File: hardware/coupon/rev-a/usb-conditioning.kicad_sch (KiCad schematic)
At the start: 18 parts, among them U24 SN74LVC2G17DBVR, U25 SN74LVC2G17DBVR, U34 TPS3808G01DBVR

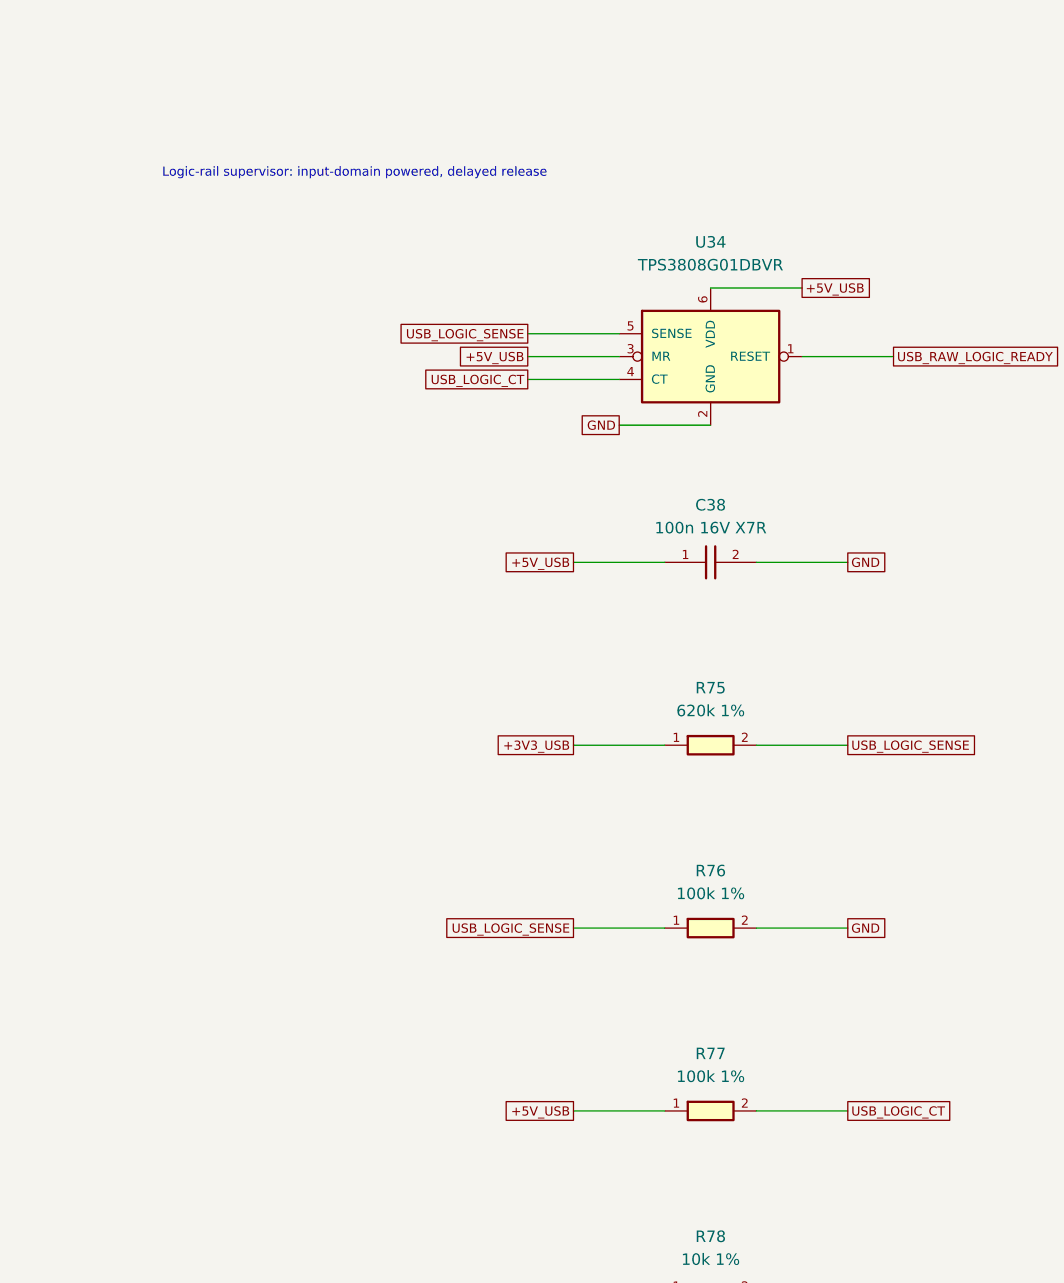
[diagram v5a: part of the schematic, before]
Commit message: Move USB supervisor to logic rail
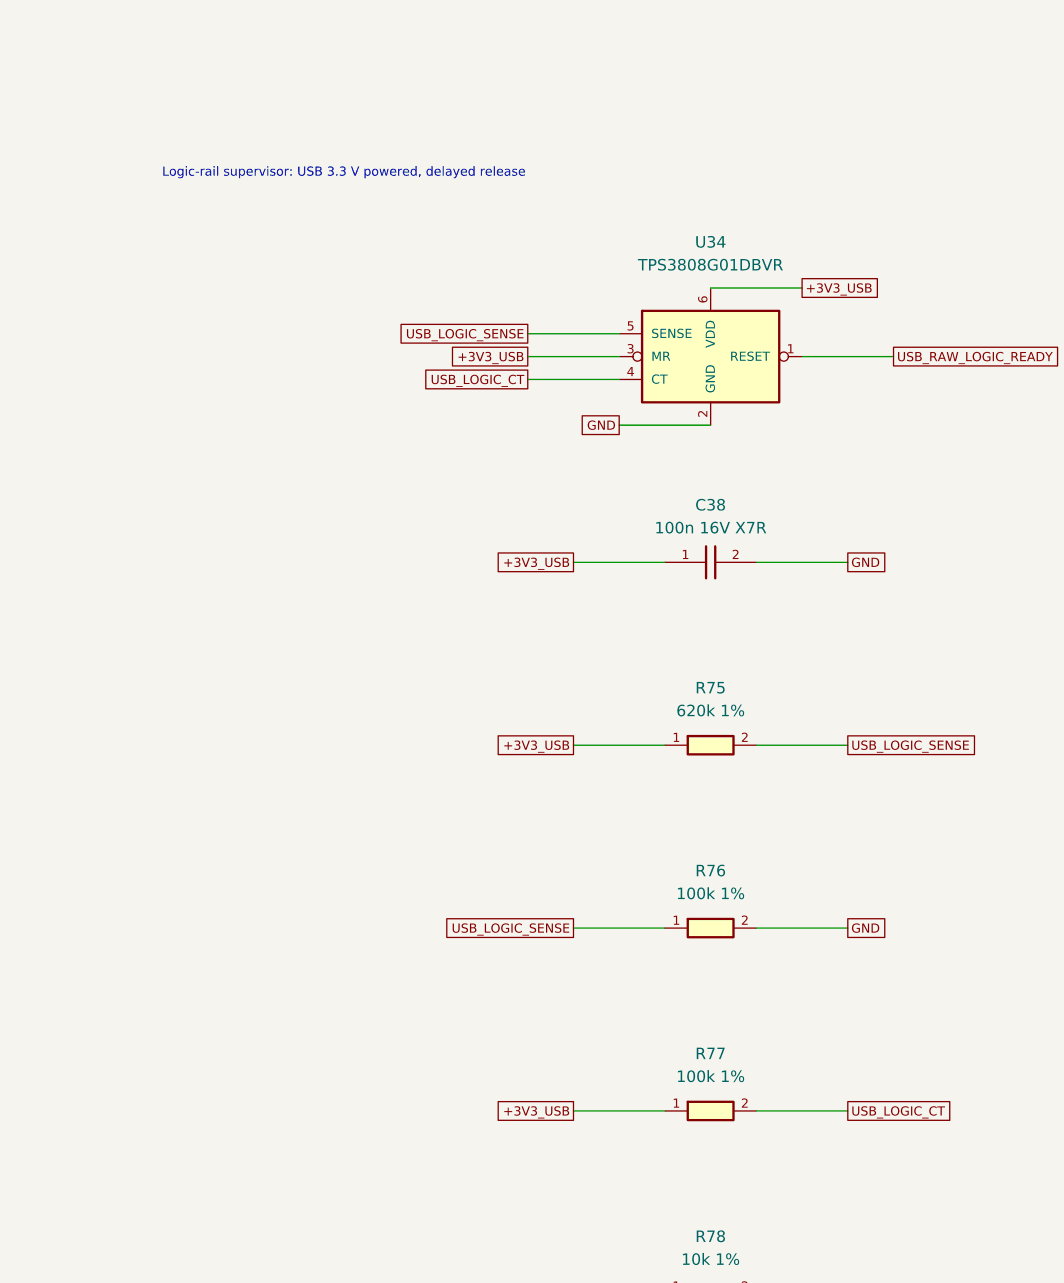
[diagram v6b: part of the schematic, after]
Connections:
- net +5V_USB is gone; now on net +3V3_USB: C38.1, R77.1, U34.3 (MR), U34.6 (VDD)
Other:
- note added: "Logic-rail supervisor: USB 3.3 V powered, delayed release"
- note removed: "Logic-rail supervisor: input-domain powered, delayed release"
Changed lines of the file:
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@@
 (wire (pts (xy 398.780 325.120) (xy 388.620 325.120)) (stroke (width 0) (type default)))
 (global_label "USB_RAW_LOGIC_READY" (shape passive) (at 388.620 325.120 180) (effects (font (size 1.016 1.016)) (justify right)) (property "Intersheetrefs" "${INTERSHEET_REFS}" (at 388.620 325.120 0) (effects (font (size 1.27 1.27)) (hide yes))))
-(text "Logic-rail supervisor: input-domain powered, delayed release" (at 383.540 175.260 0) (effects (font (size 1.016 1.016)) (justify left)))
+(text "Logic-rail supervisor: USB 3.3 V powered, delayed release" (at 383.540 175.260 0) (effects (font (size 1.016 1.016)) (justify left)))
 (symbol (lib_id "rgb-badge-coupon:TPS3808G01DBVR") (at 444.500 195.580 0) (unit 1)
 (exclude_from_sim no) (in_bom yes) (on_board yes) (dnp no)
@@
 (global_label "GND" (shape passive) (at 434.340 203.200 180) (effects (font (size 1.016 1.016)) (justify right)) (property "Intersheetrefs" "${INTERSHEET_REFS}" (at 434.340 203.200 0) (effects (font (size 1.27 1.27)) (hide yes))))
 (wire (pts (xy 434.340 195.580) (xy 424.180 195.580)) (stroke (width 0) (type default)))
-(global_label "+5V_USB" (shape passive) (at 424.180 195.580 180) (effects (font (size 1.016 1.016)) (justify right)) (property "Intersheetrefs" "${INTERSHEET_REFS}" (at 424.180 195.580 0) (effects (font (size 1.27 1.27)) (hide yes))))
+(global_label "+3V3_USB" (shape passive) (at 424.180 195.580 180) (effects (font (size 1.016 1.016)) (justify right)) (property "Intersheetrefs" "${INTERSHEET_REFS}" (at 424.180 195.580 0) (effects (font (size 1.27 1.27)) (hide yes))))
 (wire (pts (xy 434.340 198.120) (xy 424.180 198.120)) (stroke (width 0) (type default)))
 (global_label "USB_LOGIC_CT" (shape passive) (at 424.180 198.120 180) (effects (font (size 1.016 1.016)) (justify right)) (property "Intersheetrefs" "${INTERSHEET_REFS}" (at 424.180 198.120 0) (effects (font (size 1.27 1.27)) (hide yes))))
@@
 (global_label "USB_LOGIC_SENSE" (shape passive) (at 424.180 193.040 180) (effects (font (size 1.016 1.016)) (justify right)) (property "Intersheetrefs" "${INTERSHEET_REFS}" (at 424.180 193.040 0) (effects (font (size 1.27 1.27)) (hide yes))))
 (wire (pts (xy 444.500 187.960) (xy 454.660 187.960)) (stroke (width 0) (type default)))
-(global_label "+5V_USB" (shape passive) (at 454.660 187.960 0) (effects (font (size 1.016 1.016)) (justify left)) (property "Intersheetrefs" "${INTERSHEET_REFS}" (at 454.660 187.960 0) (effects (font (size 1.27 1.27)) (hide yes))))
+(global_label "+3V3_USB" (shape passive) (at 454.660 187.960 0) (effects (font (size 1.016 1.016)) (justify left)) (property "Intersheetrefs" "${INTERSHEET_REFS}" (at 454.660 187.960 0) (effects (font (size 1.27 1.27)) (hide yes))))
 (symbol (lib_id "rgb-badge-coupon:GRM155R71C104KA88D") (at 444.500 218.440 0) (unit 1)
 (exclude_from_sim no) (in_bom yes) (on_board yes) (dnp no)
@@
 (instances (project "rgb-badge-coupon" (path "/207fb68e-2ddb-46bb-8712-eba2f8c5eef6/05e96674-5624-545e-aef0-a1af37c3f4ba" (reference "C38") (unit 1)))))
 (wire (pts (xy 439.420 218.440) (xy 429.260 218.440)) (stroke (width 0) (type default)))
-(global_label "+5V_USB" (shape passive) (at 429.260 218.440 180) (effects (font (size 1.016 1.016)) (justify right)) (property "Intersheetrefs" "${INTERSHEET_REFS}" (at 429.260 218.440 0) (effects (font (size 1.27 1.27)) (hide yes))))
+(global_label "+3V3_USB" (shape passive) (at 429.260 218.440 180) (effects (font (size 1.016 1.016)) (justify right)) (property "Intersheetrefs" "${INTERSHEET_REFS}" (at 429.260 218.440 0) (effects (font (size 1.27 1.27)) (hide yes))))
 (wire (pts (xy 449.580 218.440) (xy 459.740 218.440)) (stroke (width 0) (type default)))
 (global_label "GND" (shape passive) (at 459.740 218.440 0) (effects (font (size 1.016 1.016)) (justify left)) (property "Intersheetrefs" "${INTERSHEET_REFS}" (at 459.740 218.440 0) (effects (font (size 1.27 1.27)) (hide yes))))
@@
 (instances (project "rgb-badge-coupon" (path "/207fb68e-2ddb-46bb-8712-eba2f8c5eef6/05e96674-5624-545e-aef0-a1af37c3f4ba" (reference "R77") (unit 1)))))
 (wire (pts (xy 439.420 279.400) (xy 429.260 279.400)) (stroke (width 0) (type default)))
-(global_label "+5V_USB" (shape passive) (at 429.260 279.400 180) (effects (font (size 1.016 1.016)) (justify right)) (property "Intersheetrefs" "${INTERSHEET_REFS}" (at 429.260 279.400 0) (effects (font (size 1.27 1.27)) (hide yes))))
+(global_label "+3V3_USB" (shape passive) (at 429.260 279.400 180) (effects (font (size 1.016 1.016)) (justify right)) (property "Intersheetrefs" "${INTERSHEET_REFS}" (at 429.260 279.400 0) (effects (font (size 1.27 1.27)) (hide yes))))
 (wire (pts (xy 449.580 279.400) (xy 459.740 279.400)) (stroke (width 0) (type default)))
 (global_label "USB_LOGIC_CT" (shape passive) (at 459.740 279.400 0) (effects (font (size 1.016 1.016)) (justify left)) (property "Intersheetrefs" "${INTERSHEET_REFS}" (at 459.740 279.400 0) (effects (font (size 1.27 1.27)) (hide yes))))

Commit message: Prepare isolated charger gate and supervisor loading
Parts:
- R63: value 100k 1% -> 1M 1%; symbol rgb-badge-coupon:ERJ2RKF1003X -> rgb-badge-coupon:ERJ2RKF1004X; MPN ERJ2RKF1003X -> ERJ2RKF1004X
- R78: value 10k 1% -> 100k 1%; symbol rgb-badge-coupon:ERJ2RKF1002X -> rgb-badge-coupon:ERJ2RKF1003X; MPN ERJ2RKF1002X -> ERJ2RKF1003X
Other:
- note added: "Most default pulls: 10k up / 100k down. RESET uses 100k up / 1M down for gate isolation."
- note removed: "Default pull-ups: 10 kohm. Default pull-downs: 100 kohm. Source/leakage/suspend budgets remain to be qualified."
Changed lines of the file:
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@@
 (wire (pts (xy 269.240 121.920) (xy 279.400 121.920)) (stroke (width 0) (type default)))
 (global_label "GND" (shape passive) (at 279.400 121.920 0) (effects (font (size 1.016 1.016)) (justify left)) (property "Intersheetrefs" "${INTERSHEET_REFS}" (at 279.400 121.920 0) (effects (font (size 1.27 1.27)) (hide yes))))
-(symbol (lib_id "rgb-badge-coupon:ERJ2RKF1003X") (at 264.160 142.240 0) (unit 1)
+(symbol (lib_id "rgb-badge-coupon:ERJ2RKF1004X") (at 264.160 142.240 0) (unit 1)
 (exclude_from_sim no) (in_bom yes) (on_board yes) (dnp no)
 (property "Reference" "R63" (at 264.160 135.890 0) (effects (font (size 1.27 1.27))))
-(property "Value" "100k 1%" (at 264.160 138.430 0) (effects (font (size 1.27 1.27))))
+(property "Value" "1M 1%" (at 264.160 138.430 0) (effects (font (size 1.27 1.27))))
 (property "Footprint" "rgb-badge-coupon:R_Panasonic_ERJ2_0402" (at 264.160 142.240 0) (effects (font (size 1.27 1.27)) (hide yes)))
-(property "Datasheet" "https://industrial.panasonic.com/cdbs/www-data/pdf/RDA0000/AOA0000C304.pdf" (at 264.160 142.240 0) (effects (font (size 1.27 1.27)) (hide yes)))
+(property "Datasheet" "https://industrial.panasonic.com/ww/products/pt/general-purpose-chip-resistors/models/ERJ2RKF1004X" (at 264.160 142.240 0) (effects (font (size 1.27 1.27)) (hide yes)))
 (property "Manufacturer" "Panasonic" (at 264.160 142.240 0) (effects (font (size 1.27 1.27)) (hide yes)))
-(property "MPN" "ERJ2RKF1003X" (at 264.160 142.240 0) (effects (font (size 1.27 1.27)) (hide yes)))
+(property "MPN" "ERJ2RKF1004X" (at 264.160 142.240 0) (effects (font (size 1.27 1.27)) (hide yes)))
 (pin "1")
 (pin "2")
@@
 (wire (pts (xy 449.580 279.400) (xy 459.740 279.400)) (stroke (width 0) (type default)))
 (global_label "USB_LOGIC_CT" (shape passive) (at 459.740 279.400 0) (effects (font (size 1.016 1.016)) (justify left)) (property "Intersheetrefs" "${INTERSHEET_REFS}" (at 459.740 279.400 0) (effects (font (size 1.27 1.27)) (hide yes))))
-(symbol (lib_id "rgb-badge-coupon:ERJ2RKF1002X") (at 444.500 299.720 0) (unit 1)
+(symbol (lib_id "rgb-badge-coupon:ERJ2RKF1003X") (at 444.500 299.720 0) (unit 1)
 (exclude_from_sim no) (in_bom yes) (on_board yes) (dnp no)
 (property "Reference" "R78" (at 444.500 293.370 0) (effects (font (size 1.27 1.27))))
-(property "Value" "10k 1%" (at 444.500 295.910 0) (effects (font (size 1.27 1.27))))
+(property "Value" "100k 1%" (at 444.500 295.910 0) (effects (font (size 1.27 1.27))))
 (property "Footprint" "rgb-badge-coupon:R_Panasonic_ERJ2_0402" (at 444.500 299.720 0) (effects (font (size 1.27 1.27)) (hide yes)))
 (property "Datasheet" "https://industrial.panasonic.com/cdbs/www-data/pdf/RDA0000/AOA0000C304.pdf" (at 444.500 299.720 0) (effects (font (size 1.27 1.27)) (hide yes)))
 (property "Manufacturer" "Panasonic" (at 444.500 299.720 0) (effects (font (size 1.27 1.27)) (hide yes)))
-(property "MPN" "ERJ2RKF1002X" (at 444.500 299.720 0) (effects (font (size 1.27 1.27)) (hide yes)))
+(property "MPN" "ERJ2RKF1003X" (at 444.500 299.720 0) (effects (font (size 1.27 1.27)) (hide yes)))
 (pin "1")
 (pin "2")
@@
 (wire (pts (xy 449.580 299.720) (xy 459.740 299.720)) (stroke (width 0) (type default)))
 (global_label "USB_RAW_LOGIC_READY" (shape passive) (at 459.740 299.720 0) (effects (font (size 1.016 1.016)) (justify left)) (property "Intersheetrefs" "${INTERSHEET_REFS}" (at 459.740 299.720 0) (effects (font (size 1.27 1.27)) (hide yes))))
-(text "Default pull-ups: 10 kohm. Default pull-downs: 100 kohm. Source/leakage/suspend budgets remain to be qualified." (at 20.320 375.920 0) (effects (font (size 1.27 1.27)) (justify left)))
+(text "Most default pulls: 10k up / 100k down. RESET uses 100k up / 1M down for gate isolation." (at 20.320 375.920 0) (effects (font (size 1.27 1.27)) (justify left)))
 (text "U34: nominal trip 2.916 V; CT via 100k selects 180-420 ms release. Fast brownout/actuator inhibition remain unproven." (at 20.320 386.080 0) (effects (font (size 1.016 1.016)) (justify left)))
 (embedded_fonts no)
